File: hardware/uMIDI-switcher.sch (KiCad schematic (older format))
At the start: 32 parts, among them U1 LM7809CT, U2 LM7809CT, U3 LM7809CT, U4 LM7809CT, X1 CONN_01X02, X14 uMIDI GPIO3, X15 LEDs, X16 uMIDI Power, X2 CONN_01X02, X3 CONN_01X02, X4 CONN_01X02

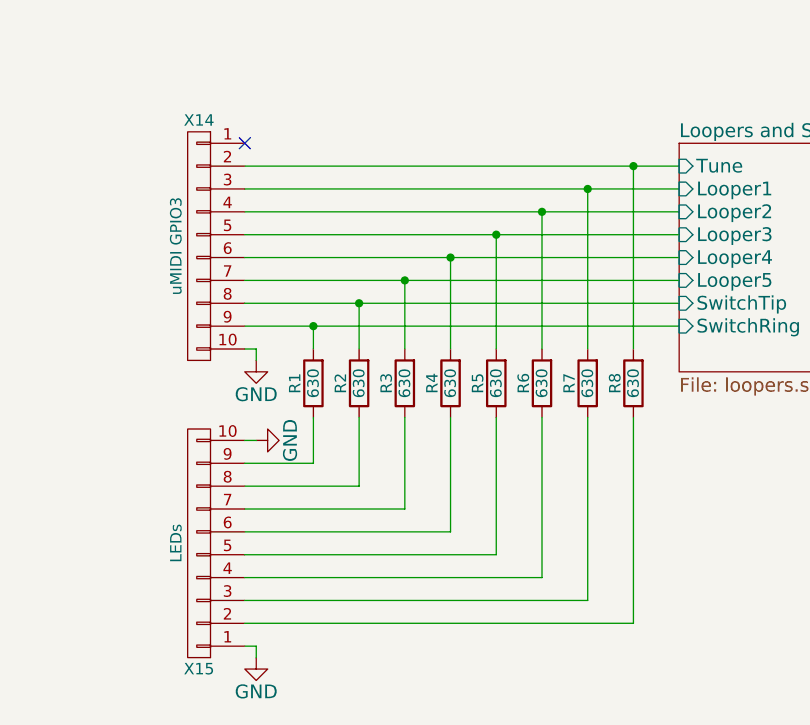
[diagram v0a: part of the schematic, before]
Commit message: Remove led distribution
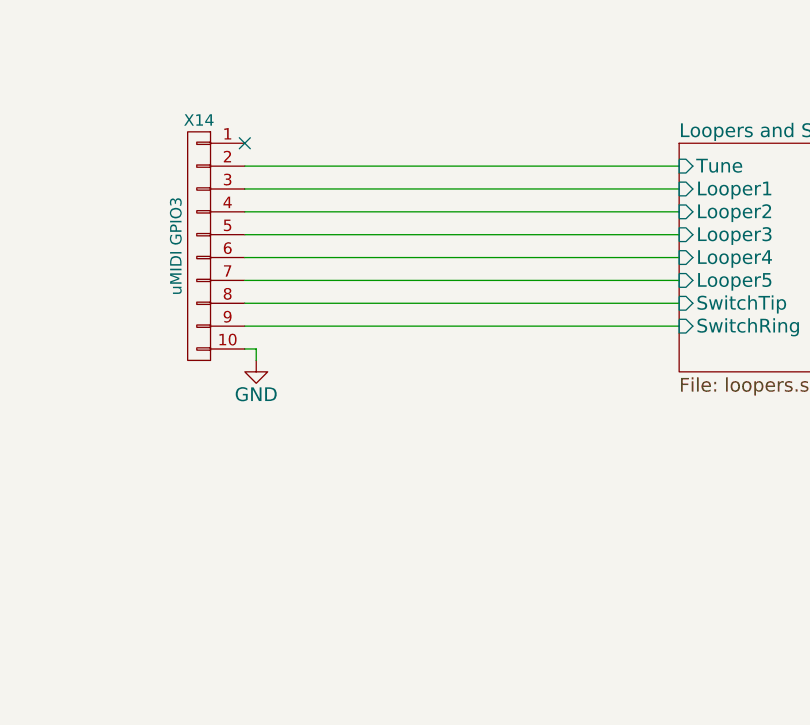
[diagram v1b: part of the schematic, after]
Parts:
- removed R1, R2, R3, R4, R5, R6, R7, R8: 630, Resistors_SMD:R_0603, symbol R
- removed X15: LEDs, Pin_Headers:Pin_Header_Straight_1x10, symbol CONN_01X10
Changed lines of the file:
@@
 LIBS:memory
 LIBS:xilinx
-LIBS:microcontrollers
-LIBS:dsp
-LIBS:microchip
-LIBS:analog_switches
-LIBS:motorola
-LIBS:texas
-LIBS:intel
-LIBS:audio
-LIBS:interface
-LIBS:digital-audio
-LIBS:philips
-LIBS:display
-LIBS:cypress
-LIBS:siliconi
-LIBS:opto
-LIBS:atmel
-LIBS:contrib
-LIBS:valves
-LIBS:stacked_jack
-LIBS:relais
-LIBS:umidi
 LIBS:uMIDI-switcher-cache
 EELAYER 25 0
@@
 	1    0    0    -1
 $EndComp
-$Comp
-L R R1
-U 1 1 55FC62EB
-P 6650 4350
-F 0 "R1" V 6730 4350 50  0000 C CNN
-F 1 "630" V 6650 4350 50  0000 C CNN
-F 2 "Resistors_SMD:R_0603" V 6580 4350 30  0001 C CNN
-F 3 "" H 6650 4350 30  0000 C CNN
-	1    6650 4350
-	-1   0    0    1
-$EndComp
-$Comp
-L GND #PWR024
-U 1 1 55FC62F7
-P 6400 5550
-F 0 "#PWR024" H 6400 5300 60  0001 C CNN
-F 1 "GND" H 6400 5400 60  0000 C CNN
-F 2 "" H 6400 5550 60  0000 C CNN
-F 3 "" H 6400 5550 60  0000 C CNN
-	1    6400 5550
-	1    0    0    -1
-$EndComp
-$Comp
-L R R2
-U 1 1 55FC630F
-P 6850 4350
-F 0 "R2" V 6930 4350 50  0000 C CNN
-F 1 "630" V 6850 4350 50  0000 C CNN
-F 2 "Resistors_SMD:R_0603" V 6780 4350 30  0001 C CNN
-F 3 "" H 6850 4350 30  0000 C CNN
-	1    6850 4350
-	-1   0    0    1
-$EndComp
-$Comp
-L R R3
-U 1 1 55FC6321
-P 7050 4350
-F 0 "R3" V 7130 4350 50  0000 C CNN
-F 1 "630" V 7050 4350 50  0000 C CNN
-F 2 "Resistors_SMD:R_0603" V 6980 4350 30  0001 C CNN
-F 3 "" H 7050 4350 30  0000 C CNN
-	1    7050 4350
-	-1   0    0    1
-$EndComp
-$Comp
-L R R4
-U 1 1 55FC6345
-P 7250 4350
-F 0 "R4" V 7330 4350 50  0000 C CNN
-F 1 "630" V 7250 4350 50  0000 C CNN
-F 2 "Resistors_SMD:R_0603" V 7180 4350 30  0001 C CNN
-F 3 "" H 7250 4350 30  0000 C CNN
-	1    7250 4350
-	-1   0    0    1
-$EndComp
-$Comp
-L R R7
-U 1 1 55FC6961
-P 7850 4350
-F 0 "R7" V 7930 4350 50  0000 C CNN
-F 1 "630" V 7850 4350 50  0000 C CNN
-F 2 "Resistors_SMD:R_0603" V 7780 4350 30  0001 C CNN
-F 3 "" H 7850 4350 30  0000 C CNN
-	1    7850 4350
-	-1   0    0    1
-$EndComp
-$Comp
-L R R5
-U 1 1 55FC6997
-P 7450 4350
-F 0 "R5" V 7530 4350 50  0000 C CNN
-F 1 "630" V 7450 4350 50  0000 C CNN
-F 2 "Resistors_SMD:R_0603" V 7380 4350 30  0001 C CNN
-F 3 "" H 7450 4350 30  0000 C CNN
-	1    7450 4350
-	-1   0    0    1
-$EndComp
-$Comp
-L R R6
-U 1 1 55FC69BB
-P 7650 4350
-F 0 "R6" V 7730 4350 50  0000 C CNN
-F 1 "630" V 7650 4350 50  0000 C CNN
-F 2 "Resistors_SMD:R_0603" V 7580 4350 30  0001 C CNN
-F 3 "" H 7650 4350 30  0000 C CNN
-	1    7650 4350
-	-1   0    0    1
-$EndComp
-$Comp
-L R R8
-U 1 1 55FC69CD
-P 8050 4350
-F 0 "R8" V 8130 4350 50  0000 C CNN
-F 1 "630" V 8050 4350 50  0000 C CNN
-F 2 "Resistors_SMD:R_0603" V 7980 4350 30  0001 C CNN
-F 3 "" H 8050 4350 30  0000 C CNN
-	1    8050 4350
-	-1   0    0    1
-$EndComp
-$Comp
-L CONN_01X10 X15
-U 1 1 55FCE5E8
-P 6150 5050
-F 0 "X15" H 6150 5600 50  0000 C CNN
-F 1 "LEDs" V 6250 5050 50  0000 C CNN
-F 2 "Pin_Headers:Pin_Header_Straight_1x10" H 6150 5050 60  0001 C CNN
-F 3 "" H 6150 5050 60  0000 C CNN
-	1    6150 5050
-	-1   0    0    1
-$EndComp
 Wire Wire Line
 	6350 4200 6400 4200
@@
 Connection ~ 3750 1300
 Wire Wire Line
-	6350 3400 8250 3400
-Wire Wire Line
 	6350 3500 8250 3500
 Wire Wire Line
@@
 Wire Wire Line
 	6350 3800 8250 3800
-Wire Wire Line
-	6650 4200 6650 4100
-Connection ~ 6650 4100
-Wire Wire Line
-	6850 4200 6850 4000
-Connection ~ 6850 4000
-Wire Wire Line
-	8050 4200 8050 3400
-Connection ~ 8050 3400
-Wire Wire Line
-	7850 4200 7850 3500
-Connection ~ 7850 3500
-Wire Wire Line
-	7650 4200 7650 3600
-Connection ~ 7650 3600
-Wire Wire Line
-	7250 4200 7250 3800
-Connection ~ 7250 3800
-Wire Wire Line
-	7050 4200 7050 3900
-Connection ~ 7050 3900
-Wire Wire Line
-	7450 4200 7450 3700
-Connection ~ 7450 3700
-Wire Wire Line
-	6350 4700 6650 4700
-Wire Wire Line
-	6650 4700 6650 4500
-Wire Wire Line
-	6350 4800 6850 4800
-Wire Wire Line
-	6850 4800 6850 4500
-Wire Wire Line
-	6350 4900 7050 4900
-Wire Wire Line
-	7050 4900 7050 4500
-Wire Wire Line
-	6350 5000 7250 5000
-Wire Wire Line
-	7250 5000 7250 4500
-Wire Wire Line
-	6350 5100 7450 5100
-Wire Wire Line
-	7450 5100 7450 4500
-Wire Wire Line
-	6350 5200 7650 5200
-Wire Wire Line
-	7650 5200 7650 4500
-Wire Wire Line
-	6350 5300 7850 5300
-Wire Wire Line
-	7850 5300 7850 4500
-Wire Wire Line
-	6350 5400 8050 5400
-Wire Wire Line
-	8050 5400 8050 4500
 $Comp
 L CONN_01X10 X14
@@
 	-1   0    0    -1
 $EndComp
-Wire Wire Line
-	6350 5500 6400 5500
-Wire Wire Line
-	6400 5500 6400 5550
-$Comp
-L GND #PWR025
-U 1 1 55FDDE2C
-P 6400 4600
-F 0 "#PWR025" H 6400 4350 60  0001 C CNN
-F 1 "GND" H 6400 4450 60  0000 C CNN
-F 2 "" H 6400 4600 60  0000 C CNN
-F 3 "" H 6400 4600 60  0000 C CNN
-	1    6400 4600
-	0    -1   -1   0
-$EndComp
-Wire Wire Line
-	6350 4600 6400 4600
 $Comp
 L CONN_01X02 X16
@@
 $EndComp
 $Comp
-L GND #PWR026
+L GND #PWR024
 U 1 1 55FDF929
 P 7000 1750
-F 0 "#PWR026" H 7000 1500 60  0001 C CNN
+F 0 "#PWR024" H 7000 1500 60  0001 C CNN
 F 1 "GND" H 7000 1600 60  0000 C CNN
 F 2 "" H 7000 1750 60  0000 C CNN
@@
 $EndComp
 $Comp
-L GND #PWR027
+L GND #PWR025
 U 1 1 55FE932A
 P 7250 1750
-F 0 "#PWR027" H 7250 1500 60  0001 C CNN
+F 0 "#PWR025" H 7250 1500 60  0001 C CNN
 F 1 "GND" H 7250 1600 60  0000 C CNN
 F 2 "" H 7250 1750 60  0000 C CNN
@@
 Connection ~ 6150 1300
 $Comp
-L GND #PWR028
+L GND #PWR026
 U 1 1 55FED47B
 P 6150 1750
-F 0 "#PWR028" H 6150 1500 60  0001 C CNN
+F 0 "#PWR026" H 6150 1500 60  0001 C CNN
 F 1 "GND" H 6150 1600 60  0000 C CNN
 F 2 "" H 6150 1750 60  0000 C CNN
@@
 	6150 1750 6150 1700
 $Comp
-L GND #PWR029
+L GND #PWR027
 U 1 1 55FED76E
 P 4450 1750
-F 0 "#PWR029" H 4450 1500 60  0001 C CNN
+F 0 "#PWR027" H 4450 1500 60  0001 C CNN
 F 1 "GND" H 4450 1600 60  0000 C CNN
 F 2 "" H 4450 1750 60  0000 C CNN
@@
 Text Label 3100 1300 0    60   ~ 0
 pwr_in
+Wire Wire Line
+	6350 3400 8250 3400
 $EndSCHEMATC

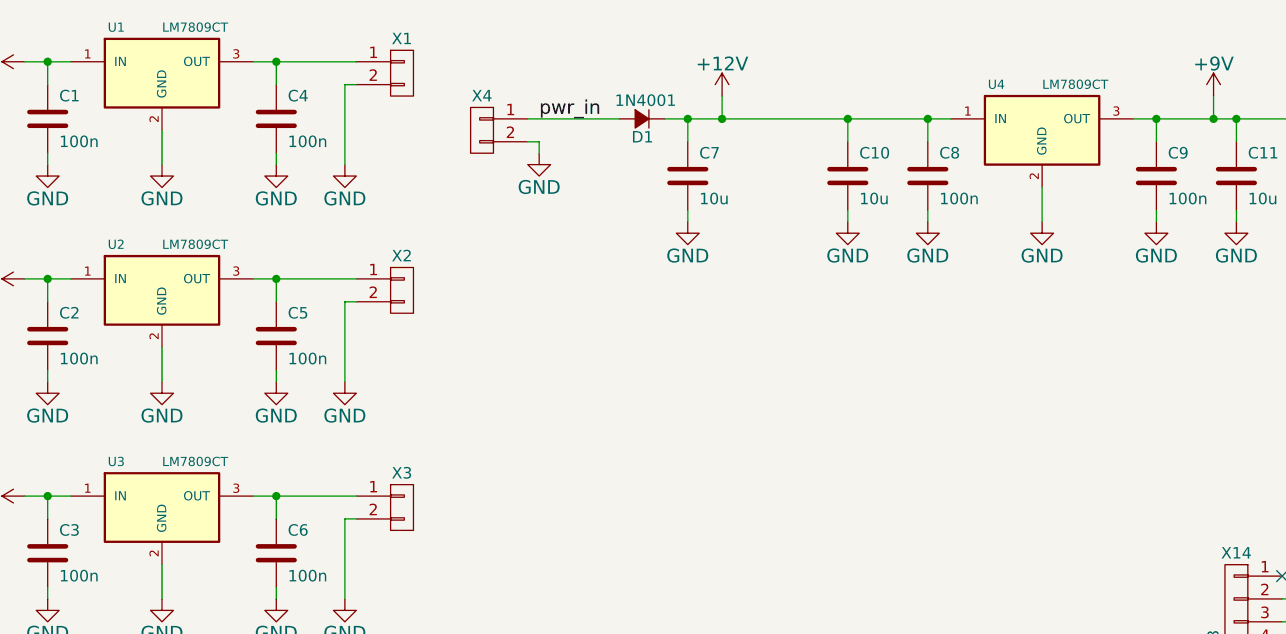
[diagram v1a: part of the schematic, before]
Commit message: Use smd regulators
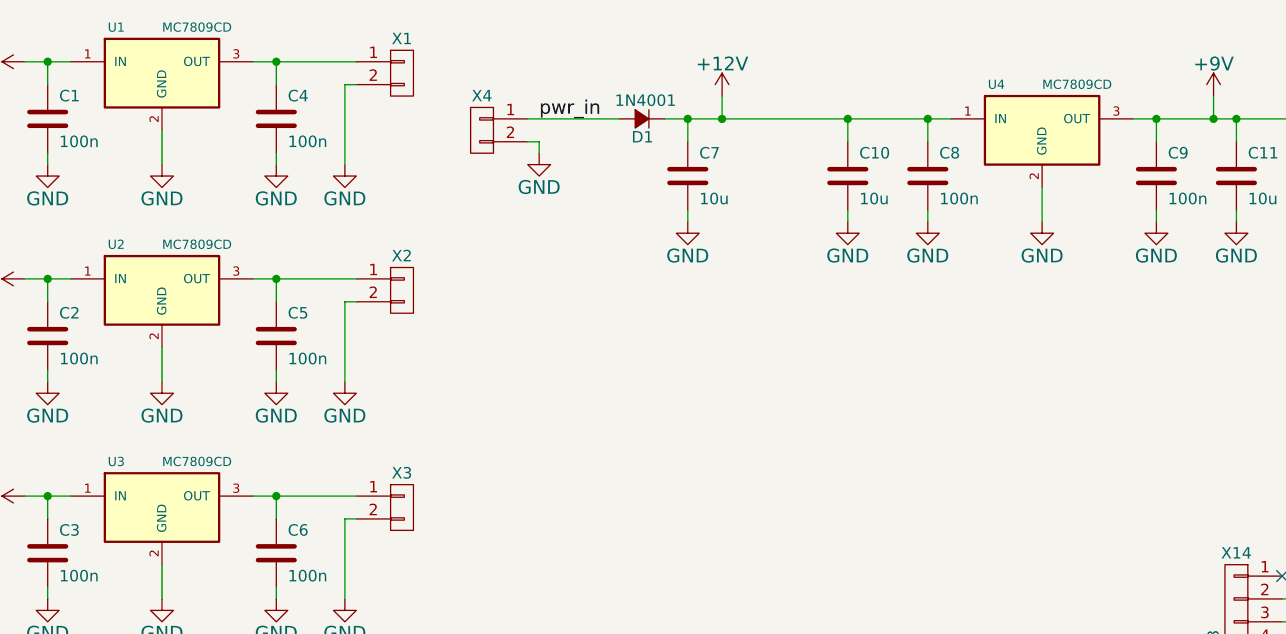
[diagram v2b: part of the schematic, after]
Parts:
- U1, U2, U3, U4: value LM7809CT -> MC7809CD; footprint Power_Integrations:TO-220 -> TO_SOT_Packages_SMD:TO-252-2Lead; Part Number LM7809CT-ND -> MC7809CD2TGOS-ND
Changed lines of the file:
@@
-$EndComp
-$Comp
-L LM7809CT U4
-U 1 1 55B6E514
-P 5300 1350
-F 0 "U4" H 5100 1550 40  0000 C CNN
-F 1 "LM7809CT" H 5300 1550 40  0000 L CNN
-F 2 "Power_Integrations:TO-220" H 5300 1450 30  0001 C CIN
-F 3 "" H 5300 1350 60  0000 C CNN
-F 4 "Digikey" H 5300 1350 60  0001 C CNN "Supplier"
-F 5 "LM7809CT-ND" H 5300 1350 60  0001 C CNN "Part Number"
-	1    5300 1350
-	1    0    0    -1
 $EndComp
 $Comp
@@
 P 1450 1100
 F 0 "U1" H 1250 1300 40  0000 C CNN
-F 1 "LM7809CT" H 1450 1300 40  0000 L CNN
-F 2 "Power_Integrations:TO-220" H 1450 1300 30  0001 C CIN
-F 3 "" H 1450 1100 60  0000 C CNN
+F 1 "MC7809CD" H 1450 1300 40  0000 L CNN
+F 2 "TO_SOT_Packages_SMD:TO-252-2Lead" H 1450 1300 30  0001 C CIN
+F 3 "http://www.onsemi.com/pub_link/Collateral/MC7800-D.PDF" H 1450 1100 60  0001 C CNN
 F 4 "Digikey" H 1450 1100 60  0001 C CNN "Supplier"
-F 5 "LM7809CT-ND" H 1450 1100 60  0001 C CNN "Part Number"
+F 5 "MC7809CD2TGOS-ND" H 1450 1100 60  0001 C CNN "Part Number"
 	1    1450 1100
 	1    0    0    -1
@@
 $EndComp
 $Comp
-L LM7809CT U2
-U 1 1 55F43678
-P 1450 2050
-F 0 "U2" H 1250 2250 40  0000 C CNN
-F 1 "LM7809CT" H 1450 2250 40  0000 L CNN
-F 2 "Power_Integrations:TO-220" H 1450 2250 30  0001 C CIN
-F 3 "" H 1450 2050 60  0000 C CNN
-F 4 "Digikey" H 1450 2050 60  0001 C CNN "Supplier"
-F 5 "LM7809CT-ND" H 1450 2050 60  0001 C CNN "Part Number"
-	1    1450 2050
-	1    0    0    -1
-$EndComp
-$Comp
 L C C5
 U 1 1 55F4367E
@@
 	1    850  2950
 	0    -1   -1   0
-$EndComp
-$Comp
-L LM7809CT U3
-U 1 1 55F437A5
-P 1450 3000
-F 0 "U3" H 1250 3200 40  0000 C CNN
-F 1 "LM7809CT" H 1450 3200 40  0000 L CNN
-F 2 "Power_Integrations:TO-220" H 1450 3200 30  0001 C CIN
-F 3 "" H 1450 3000 60  0000 C CNN
-F 4 "Digikey" H 1450 3000 60  0001 C CNN "Supplier"
-F 5 "LM7809CT-ND" H 1450 3000 60  0001 C CNN "Part Number"
-	1    1450 3000
-	1    0    0    -1
 $EndComp
 $Comp
@@
 Wire Wire Line
 	6350 3400 8250 3400
+$Comp
+L LM7809CT U2
+U 1 1 56212BE2
+P 1450 2050
+F 0 "U2" H 1250 2250 40  0000 C CNN
+F 1 "MC7809CD" H 1450 2250 40  0000 L CNN
+F 2 "TO_SOT_Packages_SMD:TO-252-2Lead" H 1450 2250 30  0001 C CIN
+F 3 "http://www.onsemi.com/pub_link/Collateral/MC7800-D.PDF" H 1450 2050 60  0001 C CNN
+F 4 "Digikey" H 1450 2050 60  0001 C CNN "Supplier"
+F 5 "MC7809CD2TGOS-ND" H 1450 2050 60  0001 C CNN "Part Number"
+	1    1450 2050
+	1    0    0    -1
+$EndComp
+$Comp
+L LM7809CT U3
+U 1 1 56212CAE
+P 1450 3000
+F 0 "U3" H 1250 3200 40  0000 C CNN
+F 1 "MC7809CD" H 1450 3200 40  0000 L CNN
+F 2 "TO_SOT_Packages_SMD:TO-252-2Lead" H 1450 3200 30  0001 C CIN
+F 3 "http://www.onsemi.com/pub_link/Collateral/MC7800-D.PDF" H 1450 3000 60  0001 C CNN
+F 4 "Digikey" H 1450 3000 60  0001 C CNN "Supplier"
+F 5 "MC7809CD2TGOS-ND" H 1450 3000 60  0001 C CNN "Part Number"
+	1    1450 3000
+	1    0    0    -1
+$EndComp
+$Comp
+L LM7809CT U4
+U 1 1 56212EDF
+P 5300 1350
+F 0 "U4" H 5100 1550 40  0000 C CNN
+F 1 "MC7809CD" H 5300 1550 40  0000 L CNN
+F 2 "TO_SOT_Packages_SMD:TO-252-2Lead" H 5300 1550 30  0001 C CIN
+F 3 "http://www.onsemi.com/pub_link/Collateral/MC7800-D.PDF" H 5300 1350 60  0001 C CNN
+F 4 "Digikey" H 5300 1350 60  0001 C CNN "Supplier"
+F 5 "MC7809CD2TGOS-ND" H 5300 1350 60  0001 C CNN "Part Number"
+	1    5300 1350
+	1    0    0    -1
+$EndComp
 $EndSCHEMATC

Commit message: Use schottky diode for input protection
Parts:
- D1: value 1N4001 -> B160; footprint Diodes_ThroughHole:Diode_DO-41_SOD81_Horizontal_RM10 -> Diodes_SMD:SMA_Standard; symbol D_Small -> D_Schottky_Small; Part Number 821-1N4001S -> B160-FDICT-ND; Supplier Mouser -> Digikey
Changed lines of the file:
@@
 Connection ~ 7000 1300
 $Comp
-L D_Small D1
+L D_Schottky_Small D1
 U 1 1 55FE235B
 P 3550 1300
-F 0 "D1" H 3500 1380 50  0000 L CNN
-F 1 "1N4001" H 3400 1220 50  0000 L CNN
-F 2 "Diodes_ThroughHole:Diode_DO-41_SOD81_Horizontal_RM10" V 3550 1300 60  0001 C CNN
+F 0 "D1" H 3500 1200 50  0000 L CNN
+F 1 "B160" H 3450 1400 50  0000 L CNN
+F 2 "Diodes_SMD:SMA_Standard" V 3550 1300 60  0001 C CNN
 F 3 "" V 3550 1300 60  0000 C CNN
-F 4 "Mouser" H 3550 1300 60  0001 C CNN "Supplier"
-F 5 "821-1N4001S " H 3550 1300 60  0001 C CNN "Part Number"
+F 4 "Digikey" H 3550 1300 60  0001 C CNN "Supplier"
+F 5 "B160-FDICT-ND" H 3550 1300 60  0001 C CNN "Part Number"
 	1    3550 1300
 	-1   0    0    1
